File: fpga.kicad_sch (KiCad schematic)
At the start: 83 parts, among them P1 JTAG_CONN, P3 mSD_CONN, Q1 BC847, Q2 BC857, SW2 SW_PUSH, SW3 SW_PUSH, U10 S25FL216K, U11 IRM-V538/TR1, U12 TLV70012, U13 TLV70025, U14 TLV70012, U2 EP4CE15E22

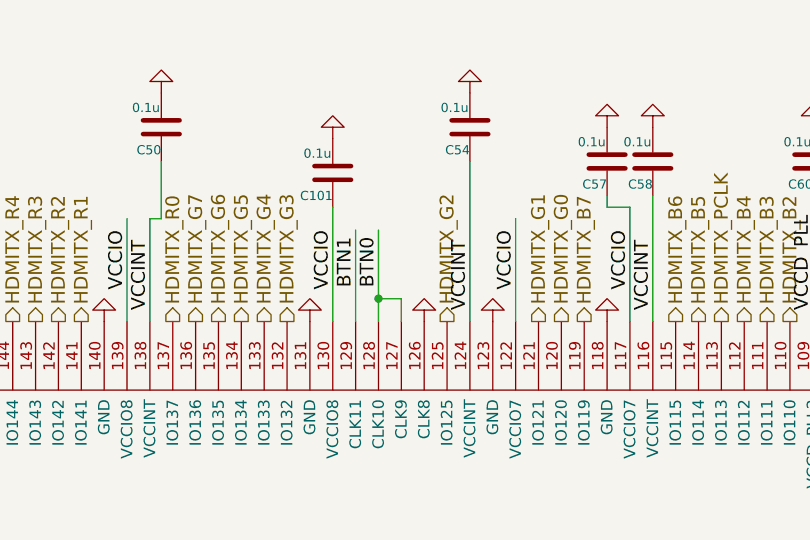
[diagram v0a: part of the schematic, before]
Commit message: change PCB version indicator pin due to conflict
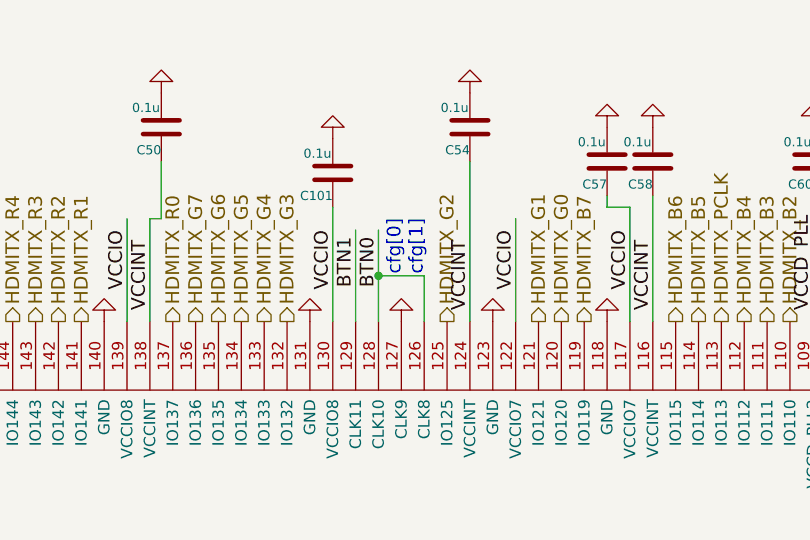
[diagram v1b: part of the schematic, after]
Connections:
- net BTN0: now also U2.126 (CLK8); no longer U2.127 (CLK9)
- net GND: now also U2.127 (CLK9); no longer U2.126 (CLK8)
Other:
- note added: "cfg[0] cfg[1]"
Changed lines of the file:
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@@
   (junction (at 177.8 29.21) (diameter 0) (color 0 0 0 0)
   )
-  (junction (at 104.14 44.45) (diameter 0) (color 0 0 0 0)
+  (junction (at 104.14 41.91) (diameter 0) (color 0 0 0 0)
   )
   (junction (at 191.77 39.37) (diameter 0) (color 0 0 0 0)
@@
     (stroke (width 0) (type default))
   )
+  (wire (pts (xy 104.14 41.91) (xy 104.14 46.99))
+    (stroke (width 0) (type default))
+  )
   (wire (pts (xy 43.18 77.47) (xy 22.86 77.47))
     (stroke (width 0) (type default))
@@
     (stroke (width 0) (type default))
   )
-  (wire (pts (xy 104.14 44.45) (xy 106.68 44.45))
-    (stroke (width 0) (type default))
-  )
   (wire (pts (xy 218.44 85.09) (xy 220.98 85.09))
     (stroke (width 0) (type default))
@@
     (stroke (width 0) (type default))
   )
+  (wire (pts (xy 109.22 41.91) (xy 104.14 41.91))
+    (stroke (width 0) (type default))
+  )
   (wire (pts (xy 40.64 92.71) (xy 43.18 92.71))
     (stroke (width 0) (type default))
@@
     (stroke (width 0) (type default))
   )
-  (wire (pts (xy 104.14 44.45) (xy 104.14 36.83))
+  (wire (pts (xy 104.14 36.83) (xy 104.14 41.91))
     (stroke (width 0) (type default))
   )
@@
     (stroke (width 0) (type default))
   )
-  (wire (pts (xy 104.14 46.99) (xy 104.14 44.45))
-    (stroke (width 0) (type default))
-  )
   (wire (pts (xy 26.67 175.26) (xy 40.64 175.26))
     (stroke (width 0) (type default))
@@
     (stroke (width 0) (type default))
   )
+  (wire (pts (xy 109.22 46.99) (xy 109.22 41.91))
+    (stroke (width 0) (type default))
+  )
   (wire (pts (xy 33.02 115.57) (xy 43.18 115.57))
     (stroke (width 0) (type default))
@@
     (stroke (width 0) (type default))
   )
-  (wire (pts (xy 106.68 44.45) (xy 106.68 46.99))
-    (stroke (width 0) (type default))
-  )
   (wire (pts (xy 33.02 110.49) (xy 43.18 110.49))
     (stroke (width 0) (type default))
@@
     (effects (font (size 1.524 1.524)) (justify left bottom))
   )
+  (text "cfg[0]\ncfg[1]" (at 109.22 41.91 90)
+    (effects (font (size 1.524 1.524)) (justify left bottom))
+  )
   (text "max. 10mA" (at 21.59 171.45 0)
     (effects (font (size 1.524 1.524)) (justify left bottom))
@@
     )
   )
-  (symbol (lib_id "power:GND") (at 109.22 46.99 180) (unit 1)
+  (symbol (lib_id "power:GND") (at 106.68 46.99 180) (unit 1)
     (in_bom yes) (on_board yes) (dnp no)
-    (property "Reference" "#PWR066" (at 109.22 46.99 0)
+    (property "Reference" "#PWR066" (at 106.68 46.99 0)
       (effects (font (size 0.762 0.762)) hide)
     )
-    (property "Value" "GND" (at 109.22 45.212 0)
+    (property "Value" "GND" (at 106.68 45.212 0)
       (effects (font (size 0.762 0.762)) hide)
     )
-    (property "Footprint" "" (at 109.22 46.99 0)
+    (property "Footprint" "" (at 106.68 46.99 0)
       (effects (font (size 1.524 1.524)) hide)
     )
-    (property "Datasheet" "" (at 109.22 46.99 0)
+    (property "Datasheet" "" (at 106.68 46.99 0)
       (effects (font (size 1.524 1.524)))
     )
